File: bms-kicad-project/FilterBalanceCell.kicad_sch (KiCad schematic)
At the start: 7 parts, among them Q13 BSS308PE_H6327

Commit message: feat: Added comment boxes and fixed 5V Regulator Schematic.
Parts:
- R?: renamed from R62; value 3k3 -> 3.3k
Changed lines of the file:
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@@
   (symbol (lib_id "FixedWing:CRCW08053K30JNEA") (at 280.67 152.4 0) (mirror y) (unit 1)
     (in_bom yes) (on_board yes) (dnp no)
-    (property "Reference" "R62" (at 271.78 149.86 0)
+    (property "Reference" "R?" (at 271.78 149.86 0)
       (effects (font (size 1.27 1.27)))
     )
-    (property "Value" "3k3" (at 271.78 152.4 0)
+    (property "Value" "3.3k" (at 271.78 152.4 0)
       (effects (font (size 1.27 1.27)))
     )
@@
       (project "bms-board"
         (path "/8a7831d1-a913-4f04-8780-225d2234b41d/95f820cc-7b9f-45ce-aa8e-ca8cb50aec5e/832e06fe-b3b7-4813-97e8-44250ee140b5"
-          (reference "R62") (unit 1)
+          (reference "R?") (unit 1)
         )
         (path "/8a7831d1-a913-4f04-8780-225d2234b41d/95f820cc-7b9f-45ce-aa8e-ca8cb50aec5e/934dcfeb-e7d5-4968-a03f-59f2aec43b96"
-          (reference "R58") (unit 1)
+          (reference "R?") (unit 1)
         )
         (path "/8a7831d1-a913-4f04-8780-225d2234b41d/95f820cc-7b9f-45ce-aa8e-ca8cb50aec5e/0cf23de6-ef6f-4a81-ad43-84518cd9ce5e"
-          (reference "R54") (unit 1)
+          (reference "R?") (unit 1)
         )
         (path "/8a7831d1-a913-4f04-8780-225d2234b41d/95f820cc-7b9f-45ce-aa8e-ca8cb50aec5e/45389985-061c-4366-94a2-f2291801023c"
-          (reference "R50") (unit 1)
+          (reference "R?") (unit 1)
         )
         (path "/8a7831d1-a913-4f04-8780-225d2234b41d/95f820cc-7b9f-45ce-aa8e-ca8cb50aec5e/b3ecb1db-76b6-4a10-9dd1-ce24dfd3cdea"
-          (reference "R46") (unit 1)
+          (reference "R?") (unit 1)
         )
         (path "/8a7831d1-a913-4f04-8780-225d2234b41d/95f820cc-7b9f-45ce-aa8e-ca8cb50aec5e/f6fcbc11-8cbd-4244-8971-29c84ec0af5d"
-          (reference "R42") (unit 1)
+          (reference "R?") (unit 1)
         )
         (path "/8a7831d1-a913-4f04-8780-225d2234b41d/95f820cc-7b9f-45ce-aa8e-ca8cb50aec5e/1f6488d5-dd45-4e35-bc3f-ca8b7492d0c2"
-          (reference "R38") (unit 1)
+          (reference "R?") (unit 1)
         )
         (path "/8a7831d1-a913-4f04-8780-225d2234b41d/95f820cc-7b9f-45ce-aa8e-ca8cb50aec5e/cf068a1a-acb0-422f-af6f-ccab6b8ceffe"
-          (reference "R34") (unit 1)
+          (reference "R?") (unit 1)
         )
         (path "/8a7831d1-a913-4f04-8780-225d2234b41d/95f820cc-7b9f-45ce-aa8e-ca8cb50aec5e/841f0fce-eb0c-41fa-958b-aa5ca04618c1"
-          (reference "R30") (unit 1)
+          (reference "R?") (unit 1)
         )
         (path "/8a7831d1-a913-4f04-8780-225d2234b41d/95f820cc-7b9f-45ce-aa8e-ca8cb50aec5e/06318de9-34c2-4095-8ab2-fa7c6761c189"
-          (reference "R26") (unit 1)
+          (reference "R?") (unit 1)
         )
         (path "/8a7831d1-a913-4f04-8780-225d2234b41d/95f820cc-7b9f-45ce-aa8e-ca8cb50aec5e/907c65e9-53f3-46a0-88c3-53aa3c395c69"
-          (reference "R22") (unit 1)
+          (reference "R?") (unit 1)
         )
         (path "/8a7831d1-a913-4f04-8780-225d2234b41d/95f820cc-7b9f-45ce-aa8e-ca8cb50aec5e/ac1001db-30e2-45f8-a5d0-23ab21f242ae"
-          (reference "R18") (unit 1)
+          (reference "R?") (unit 1)
         )
       )

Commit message: feat: Added snubber circuit to 5V Regulator schematic
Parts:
- gave numbers to parts that had none: 1
- renumbered C31 to C13, Q13 to Q12, R59 to R46, R60 to R47, R61 to R48

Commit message: feat: Added 0OHM jumper between ULTRASONIC and VDD, added LED indicator for PGOOD
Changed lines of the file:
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@@
     (stroke (width 0) (type default))
   )
-  (wire (pts (xy 148.59 139.7) (xy 142.24 139.7))
+  (wire (pts (xy 139.7 139.7) (xy 148.59 139.7))
     (stroke (width 0) (type default))
   )
@@
     (stroke (width 0) (type default))
   )
-  (wire (pts (xy 128.27 139.7) (xy 120.65 139.7))
+  (wire (pts (xy 132.08 139.7) (xy 120.65 139.7))
     (stroke (width 0) (type default))
   )
@@
     (effects (font (size 1.27 1.27)) (justify left))
   )
-  (symbol (lib_id "FixedWing:LTST-C170KRKT") (at 128.27 139.7 0) (unit 1)
+  (symbol (lib_id "FixedWing:LTST-C170KRKT") (at 132.08 139.7 0) (unit 1)
     (in_bom yes) (on_board yes) (dnp no)
     (property "Reference" "LED12" (at 135.89 143.51 0)
@@
       (effects (font (size 1.27 1.27)))
     )
-    (property "Footprint" "LEDC2012X120N" (at 140.97 233.35 0)
+    (property "Footprint" "LEDC2012X120N" (at 144.78 233.35 0)
       (effects (font (size 1.27 1.27)) (justify left bottom) hide)
     )
-    (property "Datasheet" "https://componentsearchengine.com/Datasheets/1/LTST-C170KRKT.pdf" (at 140.97 333.35 0)
+    (property "Datasheet" "https://componentsearchengine.com/Datasheets/1/LTST-C170KRKT.pdf" (at 144.78 333.35 0)
       (effects (font (size 1.27 1.27)) (justify left bottom) hide)
     )
-    (property "Height" "1.2" (at 140.97 533.35 0)
+    (property "Height" "1.2" (at 144.78 533.35 0)
       (effects (font (size 1.27 1.27)) (justify left bottom) hide)
     )
-    (property "Mouser Part Number" "859-LTST-C170KRKT" (at 140.97 633.35 0)
+    (property "Mouser Part Number" "859-LTST-C170KRKT" (at 144.78 633.35 0)
       (effects (font (size 1.27 1.27)) (justify left bottom) hide)
     )
-    (property "Mouser Price/Stock" "https://www.mouser.co.uk/ProductDetail/Lite-On/LTST-C170KRKT?qs=NUb82WqeCyrVOID%2Fxt4rgA%3D%3D" (at 140.97 733.35 0)
+    (property "Mouser Price/Stock" "https://www.mouser.co.uk/ProductDetail/Lite-On/LTST-C170KRKT?qs=NUb82WqeCyrVOID%2Fxt4rgA%3D%3D" (at 144.78 733.35 0)
       (effects (font (size 1.27 1.27)) (justify left bottom) hide)
     )
-    (property "Manufacturer_Name" "Lite-On" (at 140.97 833.35 0)
+    (property "Manufacturer_Name" "Lite-On" (at 144.78 833.35 0)
       (effects (font (size 1.27 1.27)) (justify left bottom) hide)
     )
-    (property "Manufacturer_Part_Number" "LTST-C170KRKT" (at 140.97 933.35 0)
+    (property "Manufacturer_Part_Number" "LTST-C170KRKT" (at 144.78 933.35 0)
       (effects (font (size 1.27 1.27)) (justify left bottom) hide)
     )

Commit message: feat: added buncha shit, refer to tasks 4 and 8
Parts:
- R72: renamed from R47; footprint FixedWing:RESC6332X70N -> FixedWing:RC2512N_VIS
- renumbered R46 to R71, R48 to R73, R49 to R74
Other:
- moved on the sheet: R72

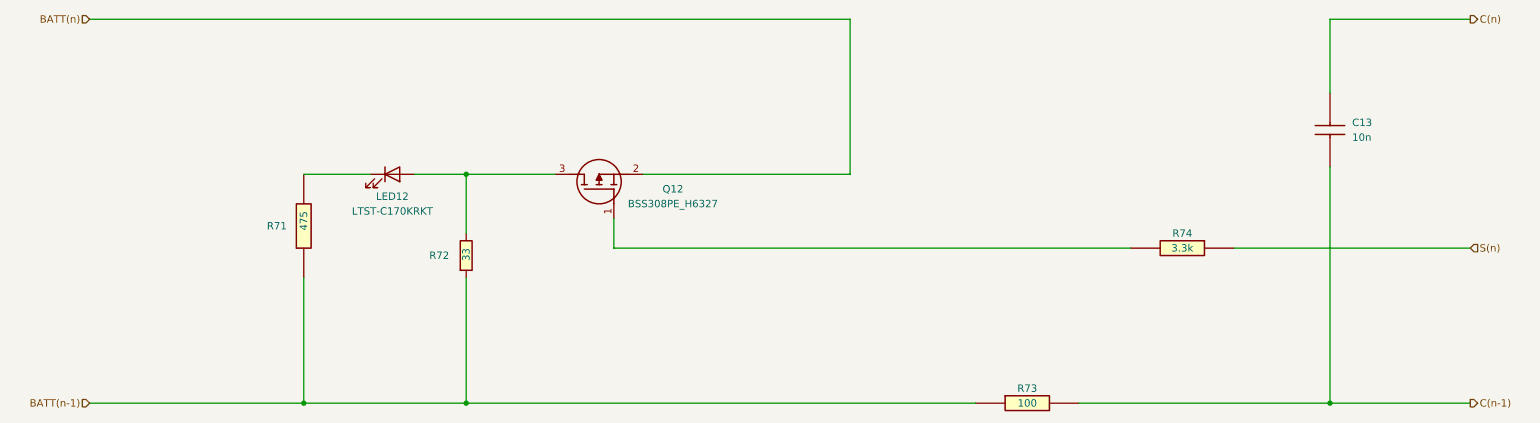
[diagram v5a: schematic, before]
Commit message: feat: finished 5V reg circuit lgtm!
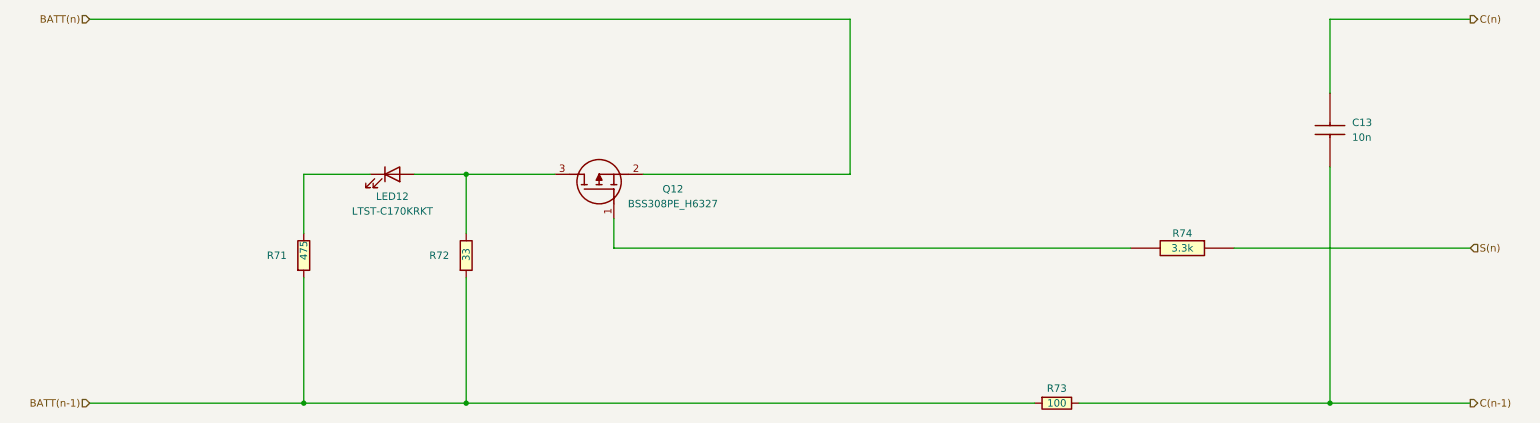
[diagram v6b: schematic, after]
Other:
- moved on the sheet: R71, R73
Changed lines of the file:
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@@
+    (stroke (width 0) (type default))
+  )
+  (wire (pts (xy 120.65 139.7) (xy 120.65 149.86))
     (stroke (width 0) (type default))
   )
@@
     (stroke (width 0) (type default))
   )
-  (wire (pts (xy 148.59 179.07) (xy 236.22 179.07))
+  (wire (pts (xy 148.59 179.07) (xy 246.38 179.07))
     (stroke (width 0) (type default))
   )
@@
     )
   )
-  (symbol (lib_id "FixedWing:CRCW0805100RFKEA") (at 236.22 179.07 0) (unit 1)
-    (in_bom yes) (on_board yes) (dnp no)
-    (property "Reference" "R73" (at 245.11 176.53 0)
-      (effects (font (size 1.27 1.27)))
-    )
-    (property "Value" "100" (at 245.11 179.07 0)
-      (effects (font (size 1.27 1.27)))
-    )
-    (property "Footprint" "RESC2012X50N" (at 250.19 275.26 0)
-      (effects (font (size 1.27 1.27)) (justify left top) hide)
-    )
-    (property "Datasheet" "http://www.vishay.com/docs/20035/dcrcwe3.pdf" (at 250.19 375.26 0)
-      (effects (font (size 1.27 1.27)) (justify left top) hide)
-    )
-    (property "Height" "0.5" (at 250.19 575.26 0)
-      (effects (font (size 1.27 1.27)) (justify left top) hide)
-    )
-    (property "Mouser Part Number" "71-CRCW0805-100-E3" (at 250.19 675.26 0)
-      (effects (font (size 1.27 1.27)) (justify left top) hide)
-    )
-    (property "Mouser Price/Stock" "https://www.mouser.co.uk/ProductDetail/Vishay-Dale/CRCW0805100RFKEA?qs=LOX6nxTstiYDPDKmuLyNLw%3D%3D" (at 250.19 775.26 0)
-      (effects (font (size 1.27 1.27)) (justify left top) hide)
-    )
-    (property "Manufacturer_Name" "Vishay" (at 250.19 875.26 0)
-      (effects (font (size 1.27 1.27)) (justify left top) hide)
-    )
-    (property "Manufacturer_Part_Number" "CRCW0805100RFKEA" (at 250.19 975.26 0)
+  (symbol (lib_id "FixedWing:CRCW0805100RFKEA") (at 246.38 179.07 0) (unit 1)
+    (in_bom yes) (on_board yes) (dnp no)
+    (property "Reference" "R73" (at 250.19 176.53 0)
+      (effects (font (size 1.27 1.27)))
+    )
+    (property "Value" "100" (at 250.19 179.07 0)
+      (effects (font (size 1.27 1.27)))
+    )
+    (property "Footprint" "RESC2012X50N" (at 260.35 275.26 0)
+      (effects (font (size 1.27 1.27)) (justify left top) hide)
+    )
+    (property "Datasheet" "http://www.vishay.com/docs/20035/dcrcwe3.pdf" (at 260.35 375.26 0)
+      (effects (font (size 1.27 1.27)) (justify left top) hide)
+    )
+    (property "Height" "0.5" (at 260.35 575.26 0)
+      (effects (font (size 1.27 1.27)) (justify left top) hide)
+    )
+    (property "Mouser Part Number" "71-CRCW0805-100-E3" (at 260.35 675.26 0)
+      (effects (font (size 1.27 1.27)) (justify left top) hide)
+    )
+    (property "Mouser Price/Stock" "https://www.mouser.co.uk/ProductDetail/Vishay-Dale/CRCW0805100RFKEA?qs=LOX6nxTstiYDPDKmuLyNLw%3D%3D" (at 260.35 775.26 0)
+      (effects (font (size 1.27 1.27)) (justify left top) hide)
+    )
+    (property "Manufacturer_Name" "Vishay" (at 260.35 875.26 0)
+      (effects (font (size 1.27 1.27)) (justify left top) hide)
+    )
+    (property "Manufacturer_Part_Number" "CRCW0805100RFKEA" (at 260.35 975.26 0)
       (effects (font (size 1.27 1.27)) (justify left top) hide)
     )
@@
   (symbol (lib_id "FixedWing:CRCW0805475RFKEA") (at 120.65 157.48 90) (unit 1)
     (in_bom yes) (on_board yes) (dnp no)
-    (property "Reference" "R71" (at 114.3 148.59 90)
+    (property "Reference" "R71" (at 114.3 153.67 90)
       (effects (font (size 1.27 1.27)) (justify right))
     )
-    (property "Value" "475" (at 120.65 146.05 0)
+    (property "Value" "475" (at 120.65 151.13 0)
       (effects (font (size 1.27 1.27)) (justify right))
     )

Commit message: Feature/library migration (#19)
* feat: first library migration commit

* feat: added sims directory, new cell balancing components

* feat: cell filtering/balancing switchover done

* feat: don't even know what I changed, just zoned out for several hours. Made PCB r/a mount XT-60s and solder pads into a 2-for-1 deal

* feat: schematic pretty much done

* feat: started layout

* feat: added current sense DAC

* feat: added capacitors to DAC

* feat:added more capacitors to DAC

* feat: more DAC capacitors

* feat: added temp sensor symbol/footprint

* added temp sense cad models

* feat: Added temp sensors

* feat: schematic cleanup, continued layout

* feat: added tvs protection ic to usb

* feat: placing cell filtering/balancing components

* feat: lotta layout

* feat: cell balancing board

* feat: changed cell balancing schem

* feat: slightly edited cell balance schem

* feat: big pre-design review schematic commit

* feat: post-design review clarity

* feat: I am so tired. 4-layer layout almost done

* feat: biiig layout and slight design change commit

* feat:bos->lax layout sesh

* feat: lax -> syd layout sesh

* feat: DRC run

* feat: deleted manufacturing files

* feat: silkscreen done

* feat: REV A COMMIT FOR FAB

* doc: updated schematic docs

---------

Co-authored-by: Ronan Gleason <gleason.r@northeastern.edu>
Co-authored-by: cassidysakamoto <sakamoto.ca@northeastern.edu>
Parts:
- C13: Manufacturer Name (none) -> YAGEO; Manufacturer Part Number (none) -> AC0805KRX7R8BB103
- LED12: Manufacturer (none) -> Lite-On; Manufacturer Part Number (none) -> LTST-C170KRKT
- Q12: Manufacturer (none) -> Infineon; Manufacturer Part Number (none) -> BSS308PE H6327
- R71: Manufacturer (none) -> Vishay; Manufacturer Part Number (none) -> CRCW0805475RFKEA
- R72: Manufacturer (none) -> Vishay; Manufacturer Part Number (none) -> CRCW251233R0FKEG
- R73: Manufacturer (none) -> Vishay; Manufacturer Part Number (none) -> CRCW0805100RFKEA
- R74: Manufacturer (none) -> Vishay; Manufacturer Part Number (none) -> CRCW08053K30JNEA
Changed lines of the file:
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@@
+      (effects (font (size 1.27 1.27)) (justify left bottom) hide)
+    )
+    (property "Manufacturer" "Lite-On" (at 144.78 833.35 0)
+      (effects (font (size 1.27 1.27)) (justify left bottom) hide)
+    )
+    (property "Manufacturer Part Number" "LTST-C170KRKT" (at 144.78 933.35 0)
       (effects (font (size 1.27 1.27)) (justify left bottom) hide)
     )
@@
       (effects (font (size 1.27 1.27)) (justify left top) hide)
     )
+    (property "Manufacturer" "Infineon" (at 872.72 135.89 0)
+      (effects (font (size 1.27 1.27)) (justify left top) hide)
+    )
+    (property "Manufacturer Part Number" "BSS308PE H6327" (at 972.72 135.89 0)
+      (effects (font (size 1.27 1.27)) (justify left top) hide)
+    )
     (pin "2")
     (pin "1")
@@
       (effects (font (size 1.27 1.27)) (justify left top) hide)
     )
+    (property "Manufacturer" "Vishay" (at 266.7 848.59 0)
+      (effects (font (size 1.27 1.27)) (justify left top) hide)
+    )
+    (property "Manufacturer Part Number" "CRCW08053K30JNEA" (at 266.7 948.59 0)
+      (effects (font (size 1.27 1.27)) (justify left top) hide)
+    )
     (pin "2")
     (pin "1")
@@
     )
     (property "Manufacturer_Part_Number" "CRCW0805100RFKEA" (at 260.35 975.26 0)
+      (effects (font (size 1.27 1.27)) (justify left top) hide)
+    )
+    (property "Manufacturer" "Vishay" (at 260.35 875.26 0)
+      (effects (font (size 1.27 1.27)) (justify left top) hide)
+    )
+    (property "Manufacturer Part Number" "CRCW0805100RFKEA" (at 260.35 975.26 0)
       (effects (font (size 1.27 1.27)) (justify left top) hide)
     )
@@
       (effects (font (size 1.27 1.27)) (justify left top) hide)
     )
+    (property "Manufacturer" "Vishay" (at 844.78 143.51 0)
+      (effects (font (size 1.27 1.27)) (justify left top) hide)
+    )
+    (property "Manufacturer Part Number" "CRCW251233R0FKEG" (at 944.78 143.51 0)
+      (effects (font (size 1.27 1.27)) (justify left top) hide)
+    )
     (pin "1")
     (pin "2")
@@
       (effects (font (size 1.27 1.27)) (justify left top) hide)
     )
+    (property "Manufacturer Name" "YAGEO" (at -399.01 134.62 0)
+      (effects (font (size 1.27 1.27)) (justify left top) hide)
+    )
+    (property "Manufacturer Part Number" "AC0805KRX7R8BB103" (at -499.01 134.62 0)
+      (effects (font (size 1.27 1.27)) (justify left top) hide)
+    )
     (pin "1")
     (pin "2")
@@
       (effects (font (size 1.27 1.27)) (justify left top) hide)
     )
+    (property "Manufacturer" "Vishay" (at 816.84 143.51 0)
+      (effects (font (size 1.27 1.27)) (justify left top) hide)
+    )
+    (property "Manufacturer Part Number" "CRCW0805475RFKEA" (at 916.84 143.51 0)
+      (effects (font (size 1.27 1.27)) (justify left top) hide)
+    )
